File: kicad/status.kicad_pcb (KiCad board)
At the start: 4 copper layers, 84.1 x 61.7 mm, 57 parts, among them J3 Conn_01x03, J4 503398-1892, J5 Bus_PCI_Express_x1, J6 USB_C_Receptacle_USB2.0_16P, U1 DM-OLED096-636, U2 RP2040, U3 MCP25625T-E/ML, U4 W25Q128JVP, X1 ABM8-272-T3, Y1 X322516MLB4SI

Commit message: added silkscreen to LCD screen pins
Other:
- board text added: "3.3V"
- board text added: "SCL"
- board text added: "SDA"
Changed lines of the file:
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@@
 	)
 	(gr_text "GND\n"
-		(at 164.93 118.94 90)
+		(at 162.43 119.19 90)
+		(layer "F.SilkS")
+		(effects
+			(font
+				(size 1 1)
+				(thickness 0.12)
+				(bold yes)
+			)
+			(justify left bottom)
+		)
+	)
+	(gr_text "SCL"
+		(at 167.59 118.89 90)
 		(layer "F.SilkS")
 		(effects
@@
 				(bold yes)
 			)
+			(justify left bottom)
+		)
+	)
+	(gr_text "SDA"
+		(at 170.13 118.87 90)
+		(layer "F.SilkS")
+		(effects
+			(font
+				(size 1 1)
+				(thickness 0.12)
+				(bold yes)
+			)
+			(justify left bottom)
+		)
+	)
+	(gr_text "3.3V"
+		(at 164.94 119.09 90)
+		(layer "F.SilkS")
+		(effects
+			(font
+				(size 1 1)
+				(thickness 0.12)
+				(bold yes)
+			)

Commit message: Updated silkscreen
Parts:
- moved R14 31.3 mm to (156.1, 111.8)
- moved D1 31.3 mm to (153.6, 111.8)
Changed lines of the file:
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@@
 	(footprint "LED_SMD:LED_0402_1005Metric"
 		(layer "F.Cu")
-		(at 132.49 88.73)
+		(at 153.605 111.79)
 		(descr "LED SMD 0402 (1005 Metric), square (rectangular) end terminal, IPC_7351 nominal, (Body size source: http://www.tortai-tech.com/upload/download/2011102023233369053.pdf), generated with kicad-footprint-generator")
 		(tags "LED")
@@
 	(footprint "Resistor_SMD:R_0402_1005Metric"
 		(layer "F.Cu")
-		(at 135.015 88.73)
+		(at 156.13 111.79)
 		(descr "Resistor SMD 0402 (1005 Metric), square (rectangular) end terminal, IPC_7351 nominal, (Body size source: IPC-SM-782 page 72, https://www.pcb-3d.com/wordpress/wp-content/uploads/ipc-sm-782a_amendment_1_and_2.pdf), generated with kicad-footprint-generator")
 		(tags "resistor")
@@
 	)
 	(gr_text "Status 0.1.0"
-		(at 129.215 87.71 0)
+		(at 150.33 110.77 0)
 		(layer "F.SilkS")
 		(effects
@@
 	)
 	(via
-		(at 149.86 111.76)
+		(at 148.23 110.29)
 		(size 0.55)
 		(drill 0.4)
@@
 	)
 	(via
-		(at 137.67 88.85)
+		(at 133.25 85.21)
 		(size 0.55)
 		(drill 0.4)
@@
 	)
 	(via
-		(at 154.94 111.76)
+		(at 151.18 111.93)
 		(size 0.55)
 		(drill 0.4)
@@
 	)
 	(segment
-		(start 136.435 88.73)
-		(end 136.4434 88.7216)
+		(start 157.55 111.79)
+		(end 157.5584 111.7816)
 		(width 0.15)
 		(layer "F.Cu")
@@
 	)
 	(segment
-		(start 135.525 88.73)
-		(end 136.435 88.73)
+		(start 156.64 111.79)
+		(end 157.55 111.79)
 		(width 0.54)
 		(layer "F.Cu")
@@
 	)
 	(via
-		(at 136.435 88.73)
+		(at 157.55 111.79)
 		(size 0.55)
 		(drill 0.4)
@@
 	)
 	(segment
-		(start 134.505 88.73)
-		(end 132.975 88.73)
+		(start 155.62 111.79)
+		(end 154.09 111.79)
 		(width 0.15)
 		(layer "F.Cu")

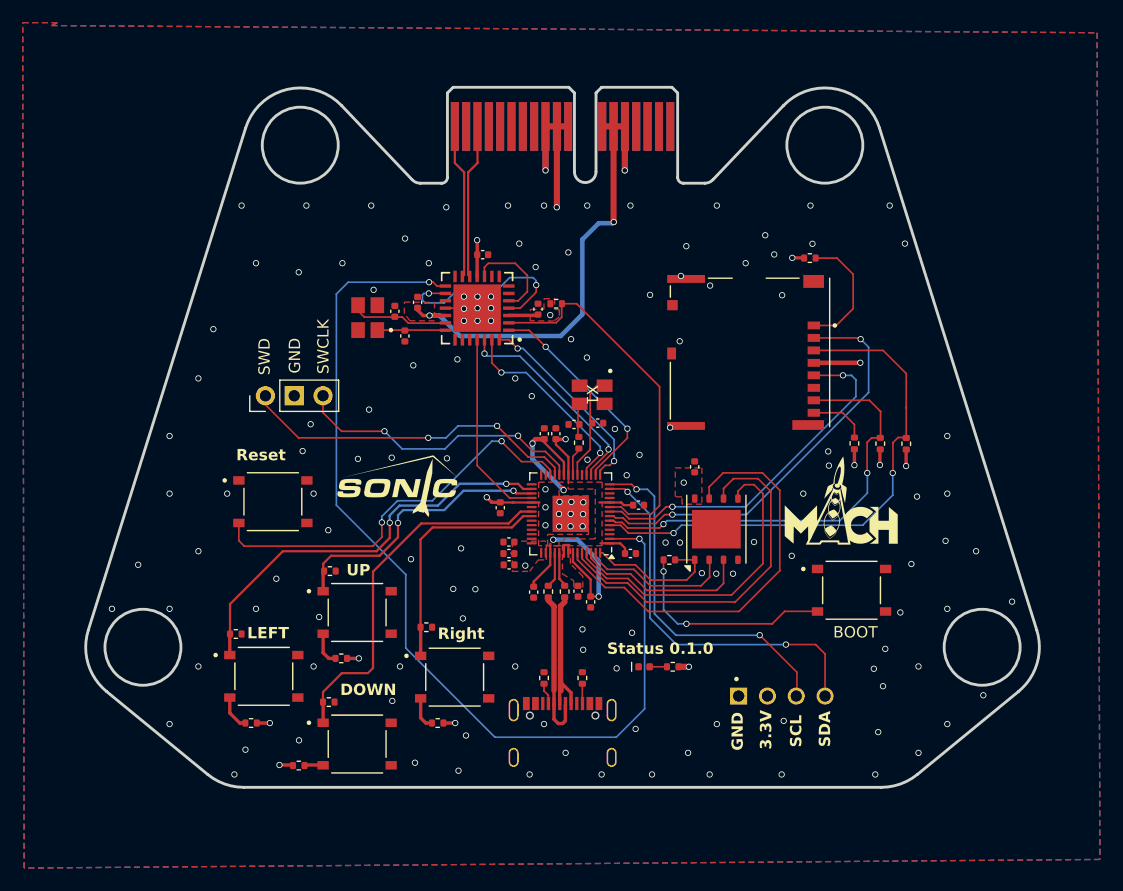
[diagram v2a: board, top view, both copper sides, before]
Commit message: Changes on the PCB layout
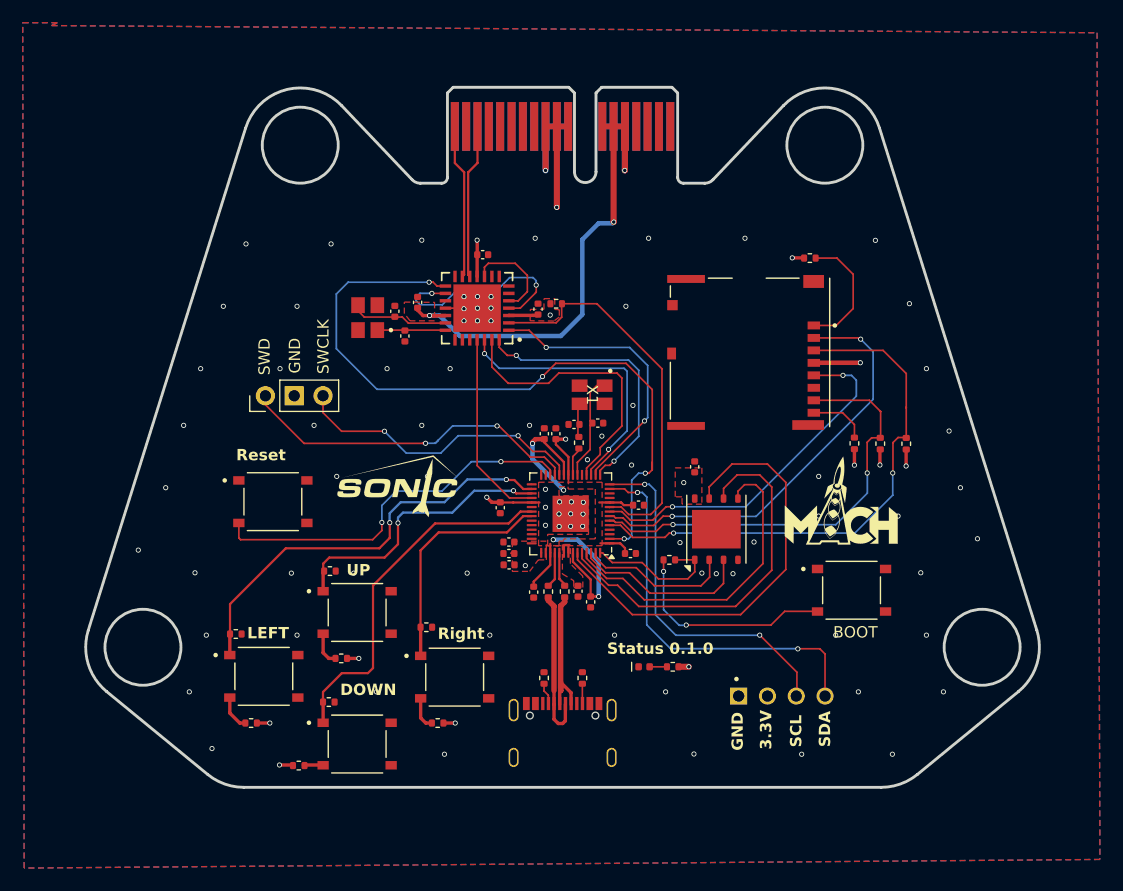
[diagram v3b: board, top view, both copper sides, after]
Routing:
- net /STBY: track 87.3 -> 63.3 mm, vias 2 -> 4
- net /MOSI_CAN: track 17.6 -> 24.8 mm, vias 2 -> 0
- net /MISO_CAN: track 17.6 -> 24.7 mm
- net /SCK_CAN: track 18.8 -> 24.9 mm
- net /CS_CAN: track 19.3 -> 25.2 mm
- net /QSPI_SD3: track 37.3 -> 39.6 mm
- net /RUN: track 35.8 -> 33.9 mm
- net /RESET: track 33.2 -> 34.5 mm
- net /SDA: track 34.1 -> 35.3 mm
- net /QSPI_CLK: track 32.5 -> 33.7 mm
- net /TX: track 17.7 -> 18.9 mm
- net /CS_SD: track 37.1 -> 38.1 mm
- net /SWD: track 30.1 -> 31.0 mm
- net /Push_Down: track 32.7 -> 32.0 mm
- net /Push_Right: track 21.7 -> 21.2 mm
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
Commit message: PCB layout changes
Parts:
- removed R9: 10K, Resistor_SMD:R_0402_1005Metric
- added R27: 1k, Resistor_SMD:R_0402_1005Metric, F.Cu at (135.4, 116.8)
- moved C15 0.27 mm to (153.1, 97.3)
- moved C8 0.10 mm to (148.8, 106.0)
- moved C23 0.09 mm to (149.4, 90.3)
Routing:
- net /TX: track 18.9 -> 15.3 mm
- net +5V: track 49.6 -> 48.6 mm
- net +1V1: track 28.1 -> 29.1 mm
- net /Push_Right: track 21.2 -> 20.4 mm
